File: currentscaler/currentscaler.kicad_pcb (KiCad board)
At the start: 2 copper layers, 30 parts, among them Q3 BC817, U1 OPA189, U2 OPA189, U3 OPA189

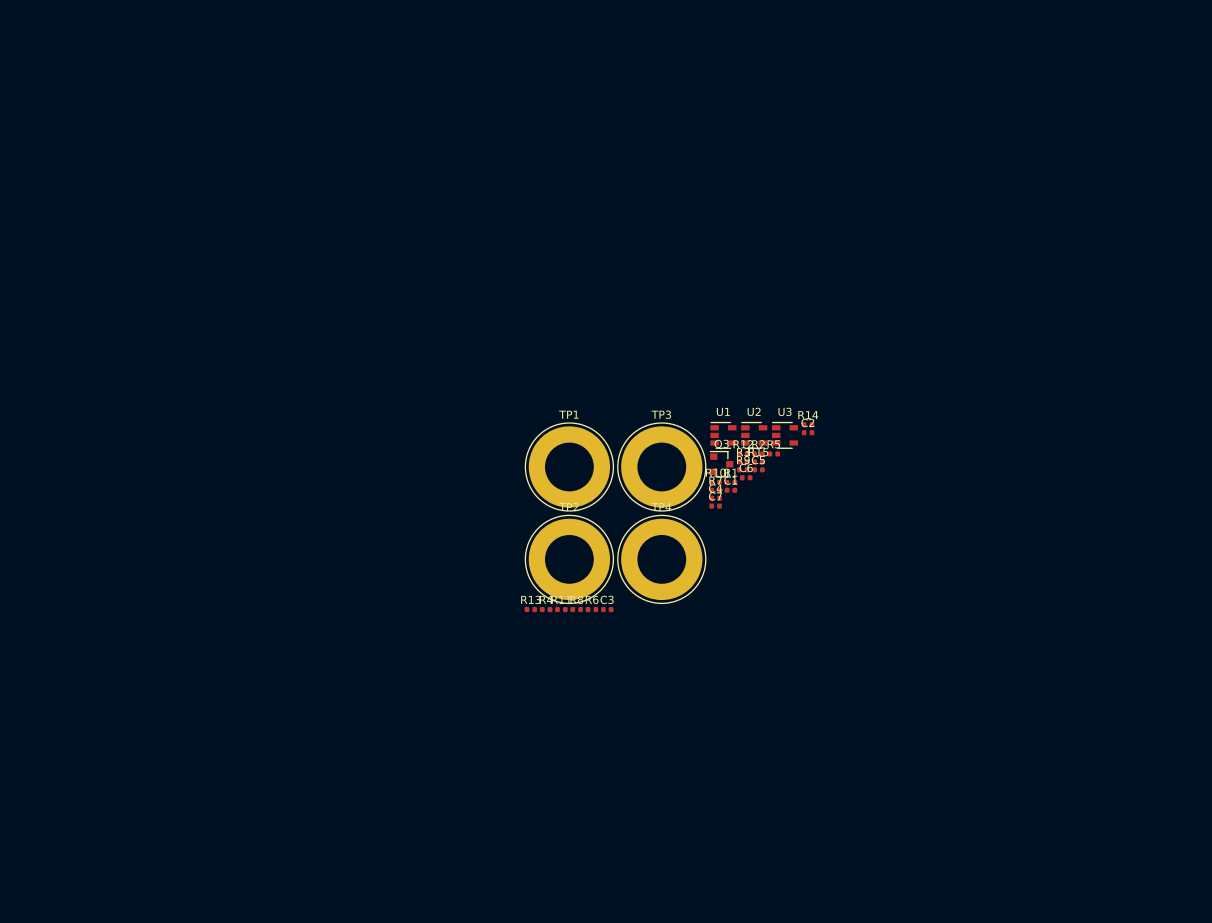
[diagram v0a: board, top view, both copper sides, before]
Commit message: Started PCB
Designing for Hammond 1550Q.
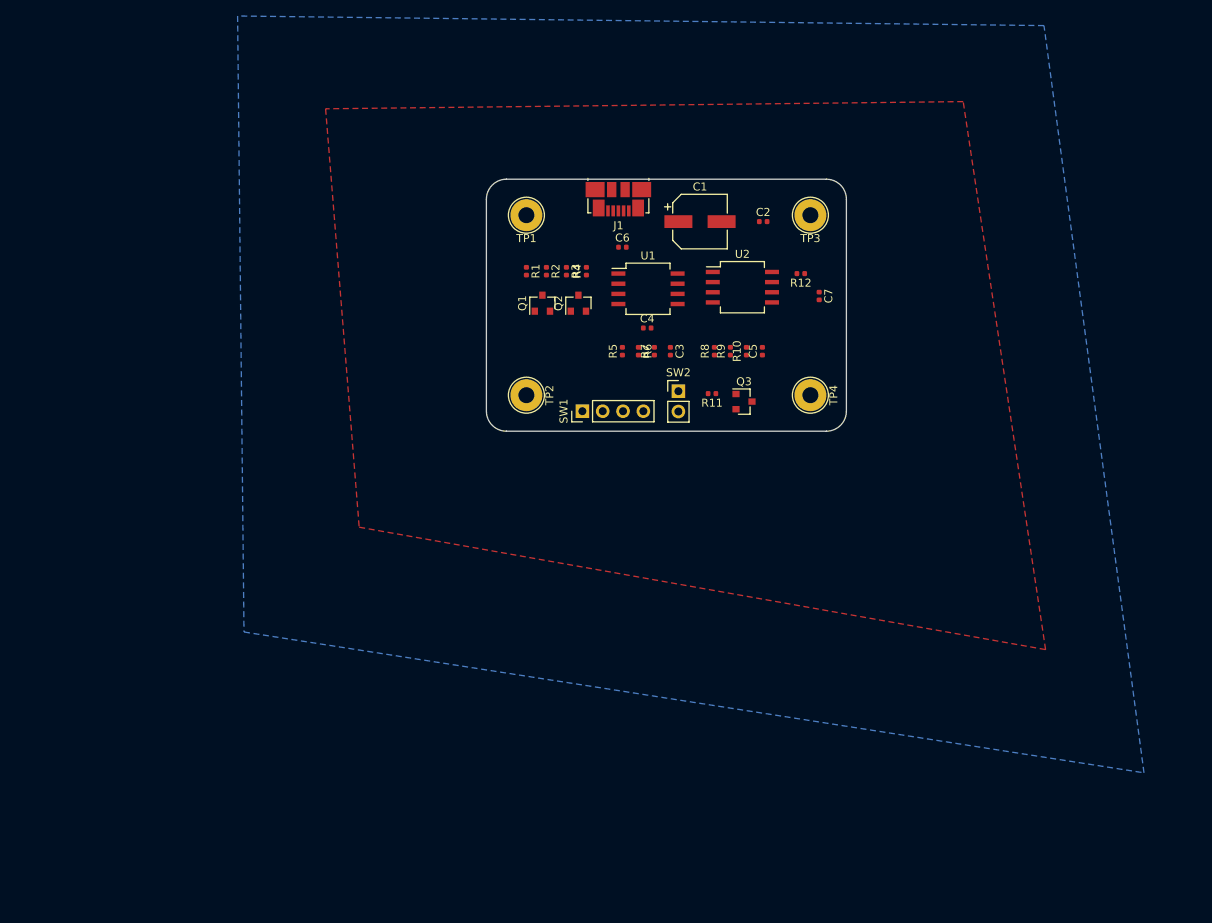
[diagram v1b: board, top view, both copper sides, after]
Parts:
- removed R13: 2.2k .05%, Resistor_SMD:R_0402_1005Metric
- removed R14: 10k, Resistor_SMD:R_0402_1005Metric
- removed R15: 220, Resistor_SMD:R_0402_1005Metric
- removed U3: OPA189, Package_TO_SOT_SMD:SOT-23-5
- added J1: USB_B, Connector_USB:USB_Micro-B_Molex_47346-0001, F.Cu at (153.0, 62.0)
- added Q1: NTR5103NT1G, Package_TO_SOT_SMD:SOT-23, F.Cu at (143.5, 75.0)
- added Q2: NTR5103NT1G, Package_TO_SOT_SMD:SOT-23, F.Cu at (148.0, 75.0)
- added SW1: SW_SP3T, Connector_PinHeader_2.54mm:PinHeader_1x04_P2.54mm_Vertical, F.Cu at (148.5, 88.5)
- added SW2: SW_SPST, Connector_PinHeader_2.54mm:PinHeader_1x02_P2.54mm_Vertical, F.Cu at (160.5, 86.0)
- C1: value 10p -> 100uF; footprint Capacitor_SMD:C_0402_1005Metric -> Capacitor_SMD:CP_Elec_6.3x7.7
- R11: value 1k .05% -> 10k
- R12: value 6.8k .05% -> 220
- TP1, TP2, TP3, TP4: footprint Connector:Banana_Jack_1Pin -> TestPoint:TestPoint_THTPad_D4.0mm_Drill2.0mm
- U1, U2: value OPA189 -> MAX4238AUT; footprint Package_TO_SOT_SMD:SOT-23-5 -> Package_SO:SO-8_5.3x6.2mm_P1.27mm
- moved R4 42.6 mm to (149.0, 71.0), turned to 90 degrees
- moved R1 36.7 mm to (141.5, 71.0), turned to 270 degrees
- moved R8 36.6 mm to (165.0, 81.0), turned to 90 degrees
- moved TP3 36.5 mm to (177.0, 64.0), turned to 180 degrees
- moved R2 35.0 mm to (144.0, 71.0), turned to 270 degrees
- moved C1 33.8 mm to (163.2, 64.8)
- moved C3 33.2 mm to (159.5, 81.0), turned to 270 degrees
- moved R11 32.9 mm to (164.7, 86.3), turned to 180 degrees
- moved R6 32.8 mm to (155.5, 81.0), turned to 270 degrees
- moved C6 32.7 mm to (153.5, 68.0)
- moved R3 32.5 mm to (146.5, 71.0), turned to 270 degrees
- moved TP1 31.9 mm to (141.5, 64.0), turned to 180 degrees
- moved C7 29.3 mm to (178.1, 74.1), turned to 270 degrees
- moved TP4 27.7 mm to (177.0, 86.5), turned to 270 degrees
- moved C2 27.0 mm to (171.1, 64.8)
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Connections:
- C1 pad 1: Net-(C1-Pad1) -> VCC
- C2 pad 1: VCC -> Net-(C1-Pad2)
- C2 pad 2: GND -> VCC
- R10 pad 1: Net-(C3-Pad1) -> Net-(C5-Pad1)
- R11 pad 1: Net-(JP2-Pad1) -> Net-(Q3-Pad1)
- R11 pad 2: Net-(C5-Pad2) -> /LP_EN
- R12 pad 1: Net-(R12-Pad1) -> Net-(C7-Pad1)
- R12 pad 2: Net-(C5-Pad2) -> Net-(C5-Pad1)
- R5 pad 2: Net-(C1-Pad2) -> Net-(C3-Pad2)
- R6 pad 2: Net-(C1-Pad2) -> Net-(C3-Pad2)
- R7 pad 1: Net-(C1-Pad1) -> Net-(C3-Pad1)
- R8 pad 2: Net-(C3-Pad2) -> Net-(C5-Pad2)
- R9 pad 2: Net-(C3-Pad2) -> Net-(C5-Pad2)
- U1 pad 1: Net-(C1-Pad1) -> VCC
- U1 pad 2: GND -> Net-(C3-Pad2)
- U1 pad 4: Net-(C1-Pad2) -> GND
- U1 pad 5: VCC -> Net-(U1-Pad5)
- U2 pad 1: Net-(C3-Pad1) -> VCC
- U2 pad 2: GND -> Net-(C5-Pad2)
- U2 pad 3: Net-(C1-Pad1) -> Net-(C3-Pad1)
- U2 pad 4: Net-(C3-Pad2) -> GND
- U2 pad 5: VCC -> Net-(U2-Pad5)
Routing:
- added copper zone on F.Cu, net GND
- added copper zone on B.Cu, net VCC
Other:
- board outline added: 45 x 31.5 mm
- board text added: "1.43 [.06]"
- board text added: "1.50 [.06]"
- board text added: "16.00 [.63]"
- board text added: "26.00 [1.02]"
- board text added: "26.80 [1.06]{ INSIDE HEIGHT}"
- board text added: "28.00 [1.10]"
- board text added: "3.00 [.12]"
- board text added: "3.47 [.14]"
- board text added: "30.10 [1.19]"
- board text added: "39.00 [1.54]"
- board text added: "4.50 [.18]"
- board text added: "43.07 [1.70]"
- board text added: "44.00 [1.73]"
- board text added: "45.00 [1.77]"
- board text added: "48.07 [1.89]"
- board text added: "4X ∅4.10 [.16]"
- board text added: "5.00 [.20]"
- board text added: "5.60 [.22]"
- board text added: "5.97 [.23]"
- board text added: "50.00 [1.97]"
- board text added: "50.74 [2.00]{ INSIDE BOX WIDTH}"
- board text added: "55.00 [2.17]"
- board text added: "55.74 [2.19]{ INSIDE BOX LENGTH}"
- board text added: "57.00 [2.24]"
- board text added: "60.00 [2.36]"
- board text added: "7.00 [.28]"
- board text added: "A"
- board text added: "B"
- board text added: "C\fSwis721 Cn BT|b1|i0;\H2.0000;"
- board text added: "Dimensions:\fArial|b0|i0;\H2.0000; mm [inches]"
- board text added: "END VIEW"
- board text added: "EVA GASKET SUPPLIED WITH LIQUID RESISTANT ENCLOSURE"
- board text added: "Enclosures can be Factory Modified ( Milling, Drilling, Printing etc.) Contact Factory mjm@hammondmfg.com for quotes Solid models of this enclosure available in STEP or IGES."
- board text added: "FILE #E65324 NEMA 4, 4X"
- board text added: "INSIDE BOX"
- board text added: "INSIDE LID"
- board text added: "L"
- board text added: "O"
- board text added: "POLYCARBONATE VERSION ONLY"
- board text added: "SECTION A-A"
- board text added: "SECTION B-B"
- board text added: "SIDE VIEW"
- board text added: "TOP VIEW"
- board text added: "U"
- board text added: "US LISTED"
- board text added: "www.hammondmfg.com"
- board text added: "{4X M3.5-0.6}"
- board text added: "®"
- board text added: "®\fCalibri|b1|i0;\H21.7410;"

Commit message: HW: rev 1 - Gerbers
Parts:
- removed C7: 100nF, Capacitor_SMD:C_0402_1005Metric
- removed J1: USB_B, Connector_USB:USB_Micro-B_Molex_47346-0001
- removed Q1, Q2: NTR5103NT1G, Package_TO_SOT_SMD:SOT-23
- removed Q3: BC817, Package_TO_SOT_SMD:SOT-23
- removed SW1: SW_SP3T, Connector_PinHeader_2.54mm:PinHeader_1x04_P2.54mm_Vertical
- removed SW2: SW_SPST, Connector_PinHeader_2.54mm:PinHeader_1x02_P2.54mm_Vertical
- added BT1: Battery_Cell, Battery:BatteryHolder_Keystone_3008_1x2450, B.Cu at (130.5, 109.5)
- added DP3T1: OS203013MT6QN1, athir:OS203013MT6QN1, F.Cu at (151.7, 99.1)
- added R13: 2.2k .05%, Resistor_SMD:R_0603_1608Metric, F.Cu at (153.8, 122.8)
- added R14: 100, Resistor_SMD:R_0603_1608Metric, F.Cu at (157.0, 108.2)
- added U3: MAX4239AUT, Package_TO_SOT_SMD:SOT-23-6, F.Cu at (145.7, 109.8)
- C1: value 100uF -> 100nF; footprint Capacitor_SMD:CP_Elec_6.3x7.7 -> Capacitor_SMD:C_0603_1608Metric
- C2, C4: value 100nF -> 10p; footprint Capacitor_SMD:C_0402_1005Metric -> Capacitor_SMD:C_0603_1608Metric
- C3, C5: value 10p -> 100nF; footprint Capacitor_SMD:C_0402_1005Metric -> Capacitor_SMD:C_0603_1608Metric
- C6: footprint Capacitor_SMD:C_0402_1005Metric -> Capacitor_SMD:C_0603_1608Metric
- R1, R10, R9: footprint Resistor_SMD:R_0402_1005Metric -> Resistor_SMD:R_0603_1608Metric
- R11: value 10k -> 1k .05%; footprint Resistor_SMD:R_0402_1005Metric -> Resistor_SMD:R_0603_1608Metric
- R12: value 220 -> 6.8k .05%; footprint Resistor_SMD:R_0402_1005Metric -> Resistor_SMD:R_0603_1608Metric
- R2: value 10 .05% -> 100k 1%; footprint Resistor_SMD:R_0402_1005Metric -> Resistor_SMD:R_0603_1608Metric
- R3: value 10m .05% -> 100k 1%; footprint Resistor_SMD:R_0402_1005Metric -> Resistor_SMD:R_0603_1608Metric
- R4: value 220 -> 10m .05%; footprint Resistor_SMD:R_0402_1005Metric -> Resistor_SMD:R_0603_1608Metric
- R5: value 1k .05% -> 10 .05%; footprint Resistor_SMD:R_0402_1005Metric -> Resistor_SMD:R_0603_1608Metric
- R6: value 6.8k .05% -> 100; footprint Resistor_SMD:R_0402_1005Metric -> Resistor_SMD:R_0603_1608Metric
- R7: value 2.2k .05% -> 1k .05%; footprint Resistor_SMD:R_0402_1005Metric -> Resistor_SMD:R_0603_1608Metric
- R8: value 1k .05% -> 100; footprint Resistor_SMD:R_0402_1005Metric -> Resistor_SMD:R_0603_1608Metric
- TP1: value SOURCE -> IN_P
- TP2: value LOAD -> IN_N
- TP3: value VOUT -> OUT_P
- TP4: value GND -> OUT_N
- U1: value MAX4238AUT -> LMV321; footprint Package_SO:SO-8_5.3x6.2mm_P1.27mm -> Package_TO_SOT_SMD:SOT-23-5
- U2: value MAX4238AUT -> MAX4239AUT; footprint Package_SO:SO-8_5.3x6.2mm_P1.27mm -> Package_TO_SOT_SMD:SOT-23-6
- moved C1 63.3 mm to (137.8, 122.8), turned to 270 degrees
- moved C2 61.8 mm to (149.8, 122.8), turned to 90 degrees
- moved R3 52.1 mm to (141.8, 122.8)
- moved R2 52.0 mm to (139.8, 122.8)
- moved TP1 51.3 mm to (104.8, 99.8)
- moved U2 49.6 mm to (147.8, 118.0), turned to 270 degrees
- moved TP2 48.9 mm to (104.8, 118.9)
- moved R12 47.3 mm to (153.0, 112.8), turned to 90 degrees
- moved U1 47.1 mm to (142.2, 118.0), turned to 90 degrees
- moved R8 46.0 mm to (145.8, 122.8)
- moved R9 46.0 mm to (147.8, 122.8)
- moved C4 44.8 mm to (155.8, 122.8), turned to 90 degrees
- moved R6 43.4 mm to (143.8, 122.8)
- moved C3 42.8 mm to (138.0, 118.0)
- moved R7 42.2 mm to (151.8, 122.8)
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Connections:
- C1 pad 1: VCC -> +9V
- C1 pad 2: Net-(C1-Pad2) -> GND
- C2 pad 1: Net-(C1-Pad2) -> Net-(C2-Pad1)
- C2 pad 2: VCC -> Net-(C2-Pad2)
- C3 pad 1: Net-(C3-Pad1) -> +9V
- C3 pad 2: Net-(C3-Pad2) -> GND
- C4 pad 1: VCC -> Net-(C4-Pad1)
- C4 pad 2: GND -> Net-(C4-Pad2)
- C5 pad 1: Net-(C5-Pad1) -> +9V
- C5 pad 2: Net-(C5-Pad2) -> GND
- C6 pad 1: VCC -> Net-(C6-Pad1)
- C6 pad 2: GND -> GNDREF
- R1 pad 1: Net-(R1-Pad1) -> Net-(DP3T1-Pad3)
- R1 pad 2: GND -> GNDREF
- R10 pad 1: Net-(C5-Pad1) -> Net-(C2-Pad1)
- R11 pad 1: Net-(Q3-Pad1) -> GNDREF
- R11 pad 2: /LP_EN -> Net-(C4-Pad2)
- R12 pad 1: Net-(C7-Pad1) -> Net-(R12-Pad1)
- R12 pad 2: Net-(C5-Pad1) -> Net-(C4-Pad2)
- R2 pad 1: Net-(R1-Pad1) -> +9V
- R2 pad 2: Net-(Q1-Pad3) -> Net-(R2-Pad2)
- R3 pad 1: Net-(R1-Pad1) -> Net-(R2-Pad2)
- R3 pad 2: Net-(Q2-Pad3) -> GND
- R4 pad 1: Net-(R4-Pad1) -> Net-(DP3T1-Pad4)
- R4 pad 2: Net-(R1-Pad1) -> GNDREF
- R5 pad 1: GND -> Net-(DP3T1-Pad2)
- R5 pad 2: Net-(C3-Pad2) -> Net-(DP3T1-Pad4)
- R6 pad 1: Net-(R6-Pad1) -> GNDREF
- R6 pad 2: Net-(C3-Pad2) -> Net-(R6-Pad2)
- R7 pad 1: Net-(C3-Pad1) -> GNDREF
- R7 pad 2: Net-(R6-Pad1) -> Net-(C2-Pad2)
- R8 pad 1: GND -> Net-(R8-Pad1)
- R8 pad 2: Net-(C5-Pad2) -> Net-(DP3T1-Pad6)
- R9 pad 2: Net-(C5-Pad2) -> Net-(C2-Pad2)
- TP1 pad 1: Net-(R1-Pad1) -> Net-(DP3T1-Pad3)
- TP2 pad 1: GND -> GNDREF
- TP3 pad 1: Net-(C7-Pad1) -> Net-(C6-Pad1)
- TP4 pad 1: GND -> GNDREF
- U1 pad 1: VCC -> Net-(R2-Pad2)
- U1 pad 2: Net-(C3-Pad2) -> GND
- U1 pad 3: Net-(R4-Pad1) -> Net-(R6-Pad2)
- U1 pad 4: GND -> Net-(R6-Pad2)
- U1 pad 5: Net-(U1-Pad5) -> +9V
- U2 pad 1: VCC -> Net-(C2-Pad1)
- U2 pad 2: Net-(C5-Pad2) -> GND
- U2 pad 3: Net-(C3-Pad1) -> Net-(R8-Pad1)
- U2 pad 4: GND -> Net-(C2-Pad2)
- U2 pad 6: Net-(C5-Pad1) -> +9V
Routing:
- net Net-(DP3T1-Pad3): track 0.00 -> 60.4 mm
- net GND: track 0.00 -> 55.5 mm, vias 0 -> 3
- net +9V: track 0.00 -> 37.9 mm, vias 0 -> 3
- net Net-(C4-Pad1): track 0.00 -> 37.2 mm
- net Net-(DP3T1-Pad4): track 0.00 -> 26.6 mm
- net Net-(C4-Pad2): track 0.00 -> 23.1 mm, vias 0 -> 2
- net Net-(C2-Pad1): track 0.00 -> 22.2 mm, vias 0 -> 3
- net GNDREF: track 0.00 -> 20.4 mm, vias 0 -> 2
- net Net-(DP3T1-Pad2): track 0.00 -> 20.0 mm, vias 0 -> 2
- net Net-(C6-Pad1): track 0.00 -> 14.0 mm
- net Net-(R6-Pad2): track 0.00 -> 12.9 mm, vias 0 -> 3
- net Net-(R10-Pad2): track 0.00 -> 11.3 mm, vias 0 -> 2
- net Net-(C2-Pad2): track 0.00 -> 10.2 mm, vias 0 -> 2
- net Net-(R8-Pad1): track 0.00 -> 9.51 mm, vias 0 -> 2
- net Net-(R12-Pad1): track 0.00 -> 8.88 mm
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- added copper zone on B.Cu, net +9V
- added copper zone on F.Cu, net GNDREF
- removed copper zone on F.Cu, net GND
- removed copper zone on B.Cu, net VCC
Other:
- board size 45 x 31.5 mm -> 76.1 x 33.4 mm
- board text added: "Current Scaler Rev 1 - 1913 ATHIR"
- board text removed: "39.00 [1.54]"
- board text removed: "44.00 [1.73]"
- board text removed: "5.00 [.20]"
- board text removed: "57.00 [2.24]"
- board text removed: "INSIDE BOX"
- board text removed: "{4X M3.5-0.6}"

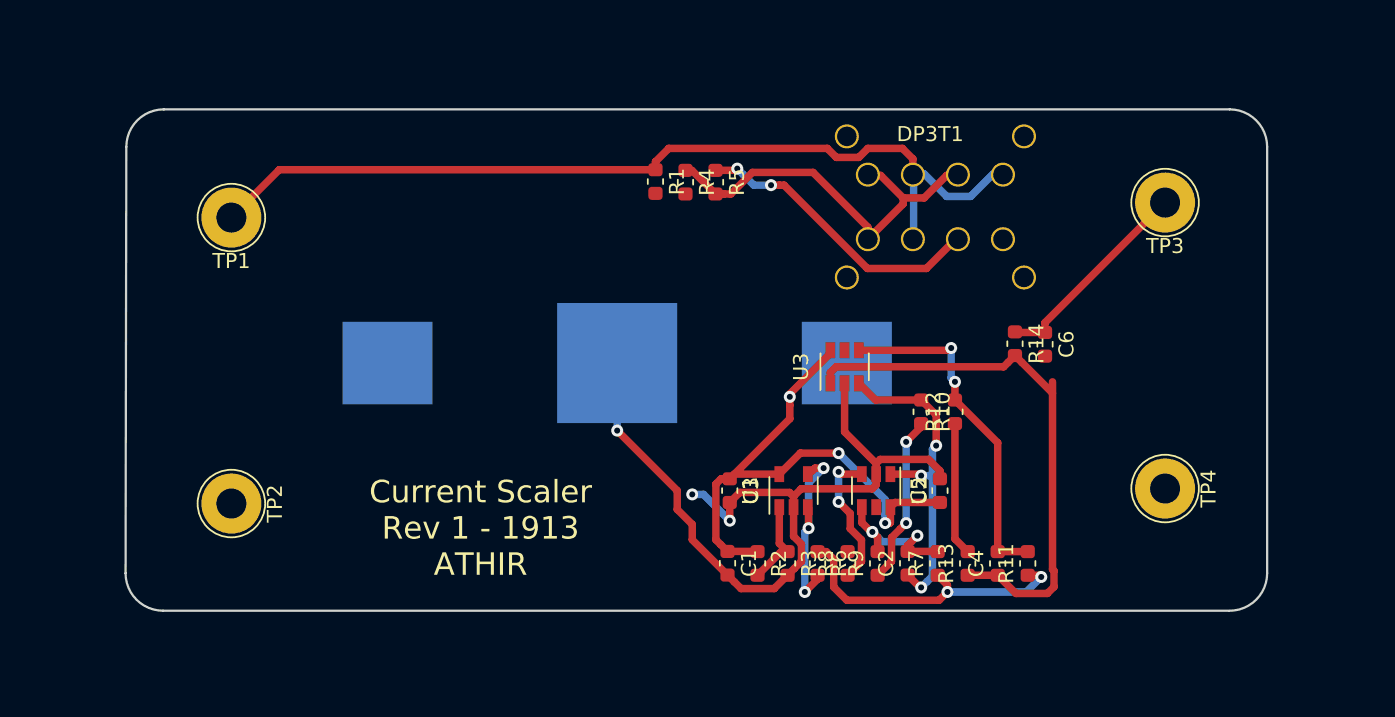
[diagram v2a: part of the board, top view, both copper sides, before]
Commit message: HW: rev 2 - Gerbers
Corrected DP3T footprint.
Added 3D file for entire PCB.
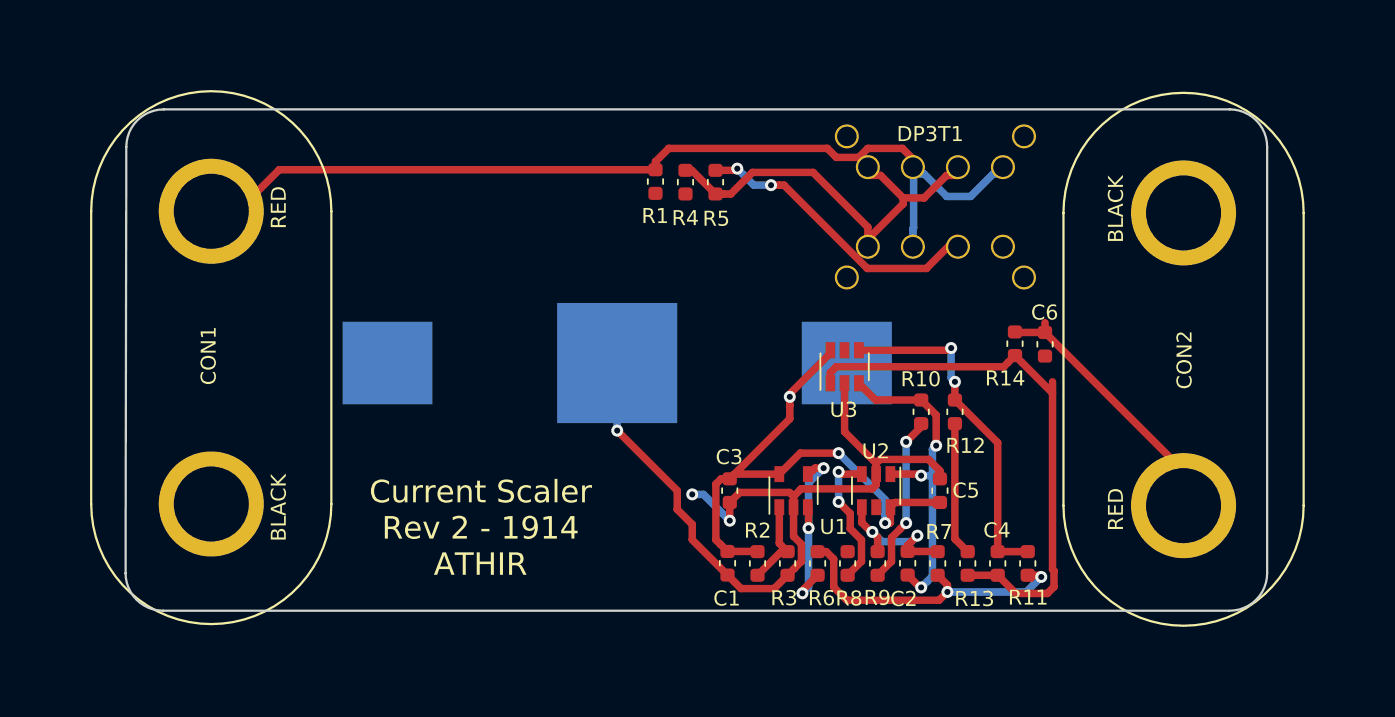
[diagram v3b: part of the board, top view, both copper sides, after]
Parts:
- removed TP1: IN_P, TestPoint:TestPoint_THTPad_D4.0mm_Drill2.0mm
- removed TP2: IN_N, TestPoint:TestPoint_THTPad_D4.0mm_Drill2.0mm
- removed TP3: OUT_P, TestPoint:TestPoint_THTPad_D4.0mm_Drill2.0mm
- removed TP4: OUT_N, TestPoint:TestPoint_THTPad_D4.0mm_Drill2.0mm
- added CON1: RS677-8759, athir:6778759, F.Cu at (103.5, 109.1)
- added CON2: RS677-8759, athir:6778759, F.Cu at (168.2, 109.2)
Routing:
- net Net-(C6-Pad1): track 14.0 -> 18.0 mm
- net Net-(CON1-Pad1): track 60.4 -> 61.6 mm
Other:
- board text added: "Current Scaler Rev 2 - 1914 ATHIR"
- board text removed: "Current Scaler Rev 1 - 1913 ATHIR"
